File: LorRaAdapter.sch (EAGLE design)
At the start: 6 parts, among them P1 PINHD-2X4, U1 WIRELESS-LORA-RFM95W#SMD

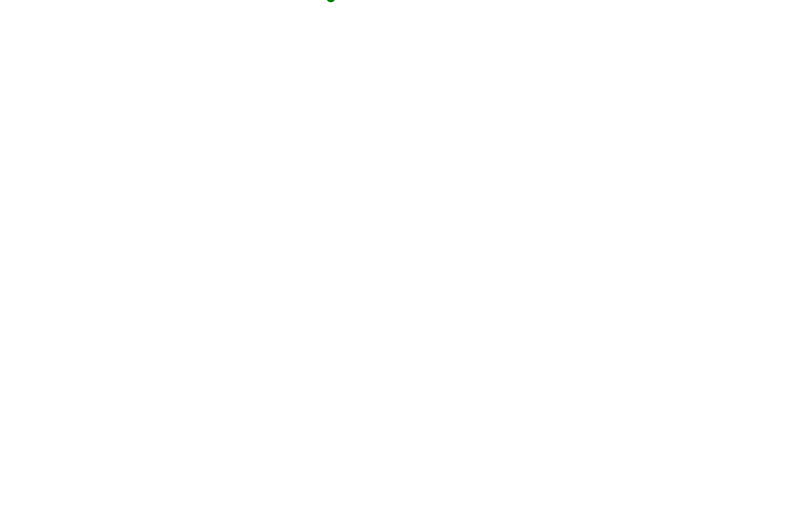
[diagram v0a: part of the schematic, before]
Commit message: Add Midnight Fog logos
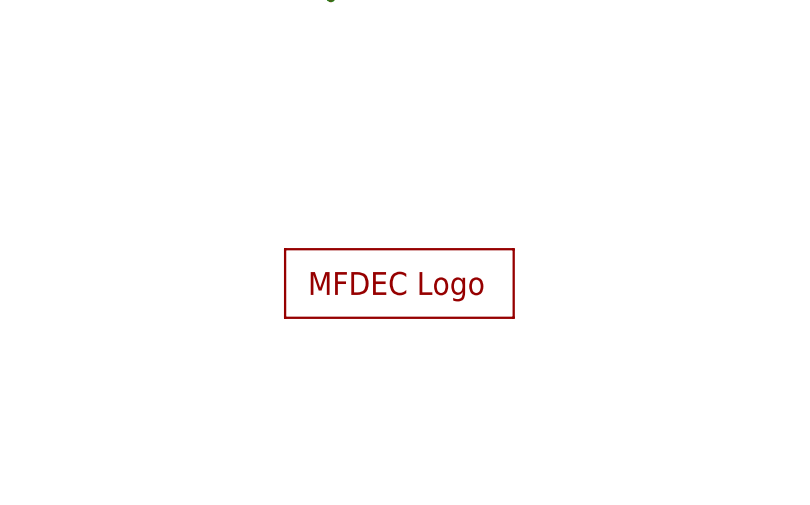
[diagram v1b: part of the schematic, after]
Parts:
- added LOGO1: MFDECLOGO_SQ_5MM, _my_logos:MFDECLOGO_SQ_5MM
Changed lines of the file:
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@@
 <part name="C1" library="rcl" library_urn="urn:adsk.eagle:library:334" deviceset="C-EU" device="C0603" package3d_urn="urn:adsk.eagle:package:23616/2" value="100nF"/>
 <part name="C2" library="rcl" library_urn="urn:adsk.eagle:library:334" deviceset="C-EU" device="C1206" package3d_urn="urn:adsk.eagle:package:23618/2" value="22uF"/>
+<part name="LOGO1" library="_my_logos" deviceset="MFDECLOGO" device="_SQ_5MM"/>
 </parts>
 <sheets>
@@
 <attribute name="VALUE" x="179.324" y="63.881" size="1.778" layer="96"/>
 </instance>
+<instance part="LOGO1" gate="G$1" x="165.1" y="25.4" smashed="yes"/>
 </instances>
 <busses>

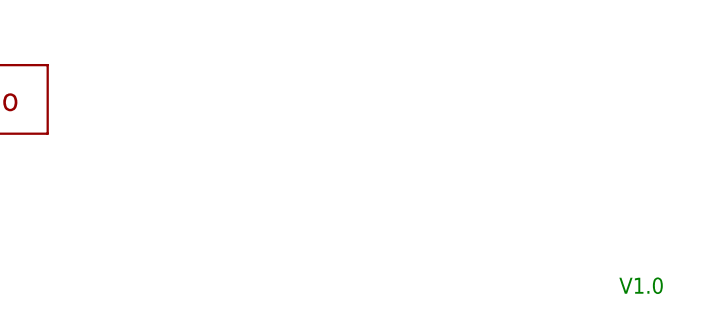
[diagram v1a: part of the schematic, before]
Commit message: Added board ids. Changed some visuals.
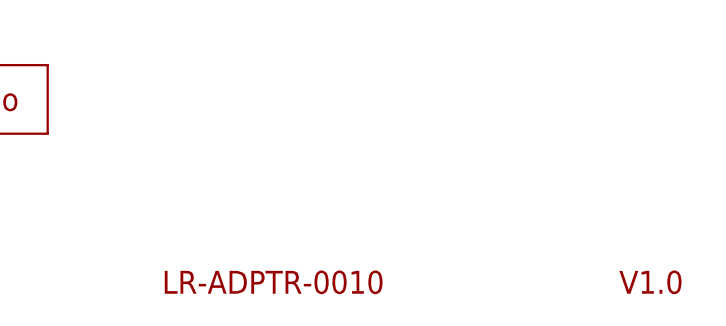
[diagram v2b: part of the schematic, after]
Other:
- note added: "LR-ADPTR-0010"
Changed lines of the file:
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@@
 <sheet>
 <plain>
-<text x="254" y="7.62" size="1.778" layer="91">V1.0</text>
+<text x="254" y="7.62" size="2.54" layer="94">V1.0</text>
+<text x="203.2" y="7.62" size="2.54" layer="94">LR-ADPTR-0010</text>
 </plain>
 <instances>
